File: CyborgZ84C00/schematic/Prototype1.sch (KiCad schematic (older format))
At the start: 13 parts, among them J1 Conn_Micro_SD, J2 Conn_I2C_Master, J3 Conn_AVR_UPDI, J4 Conn_USB_Serial, U1 Z84C00, U2 ATmega4809-P, U3 HM628128

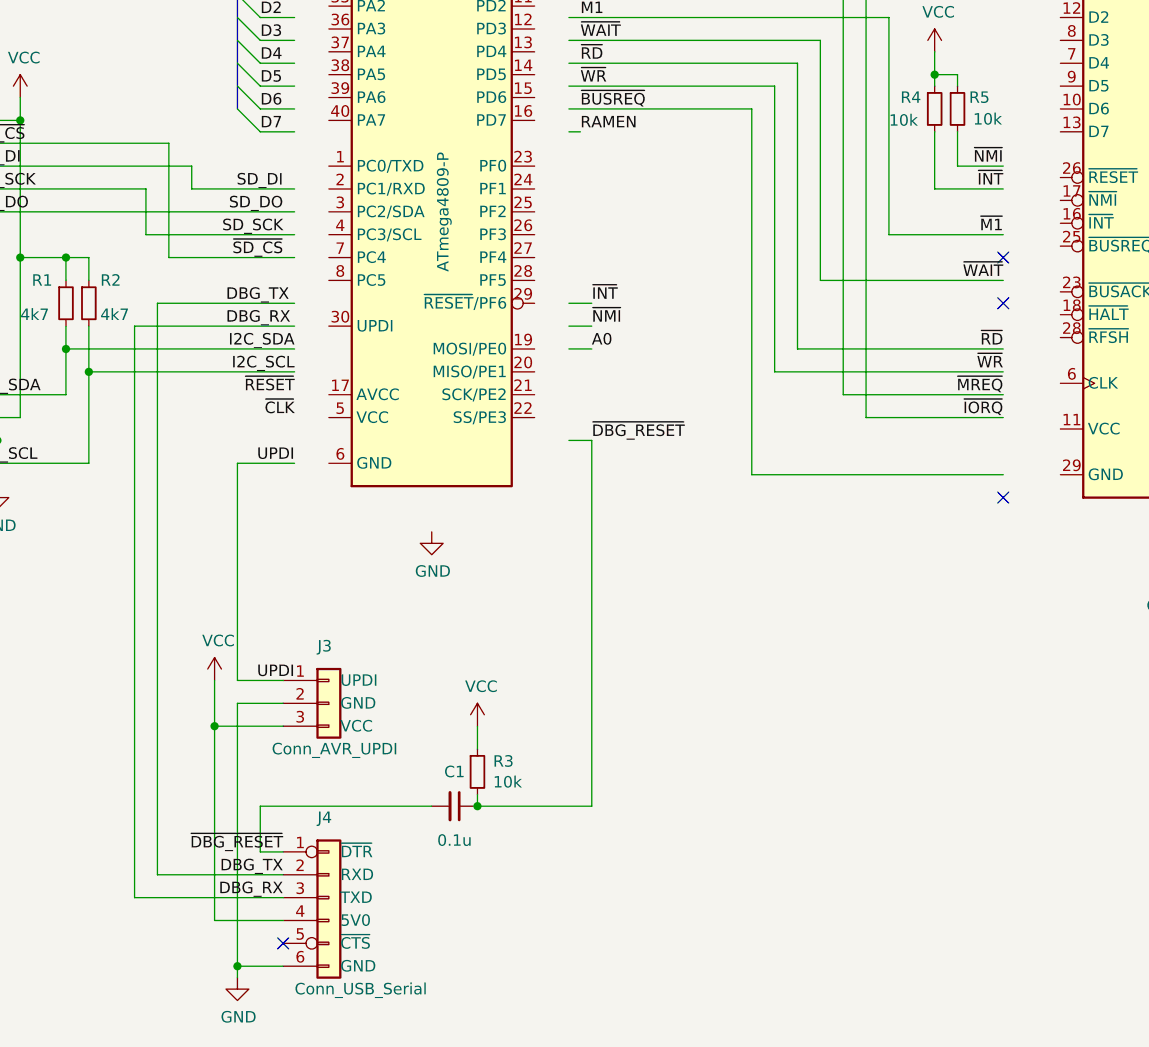
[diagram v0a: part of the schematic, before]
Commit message: [CyborgZ84C00] update debugger code
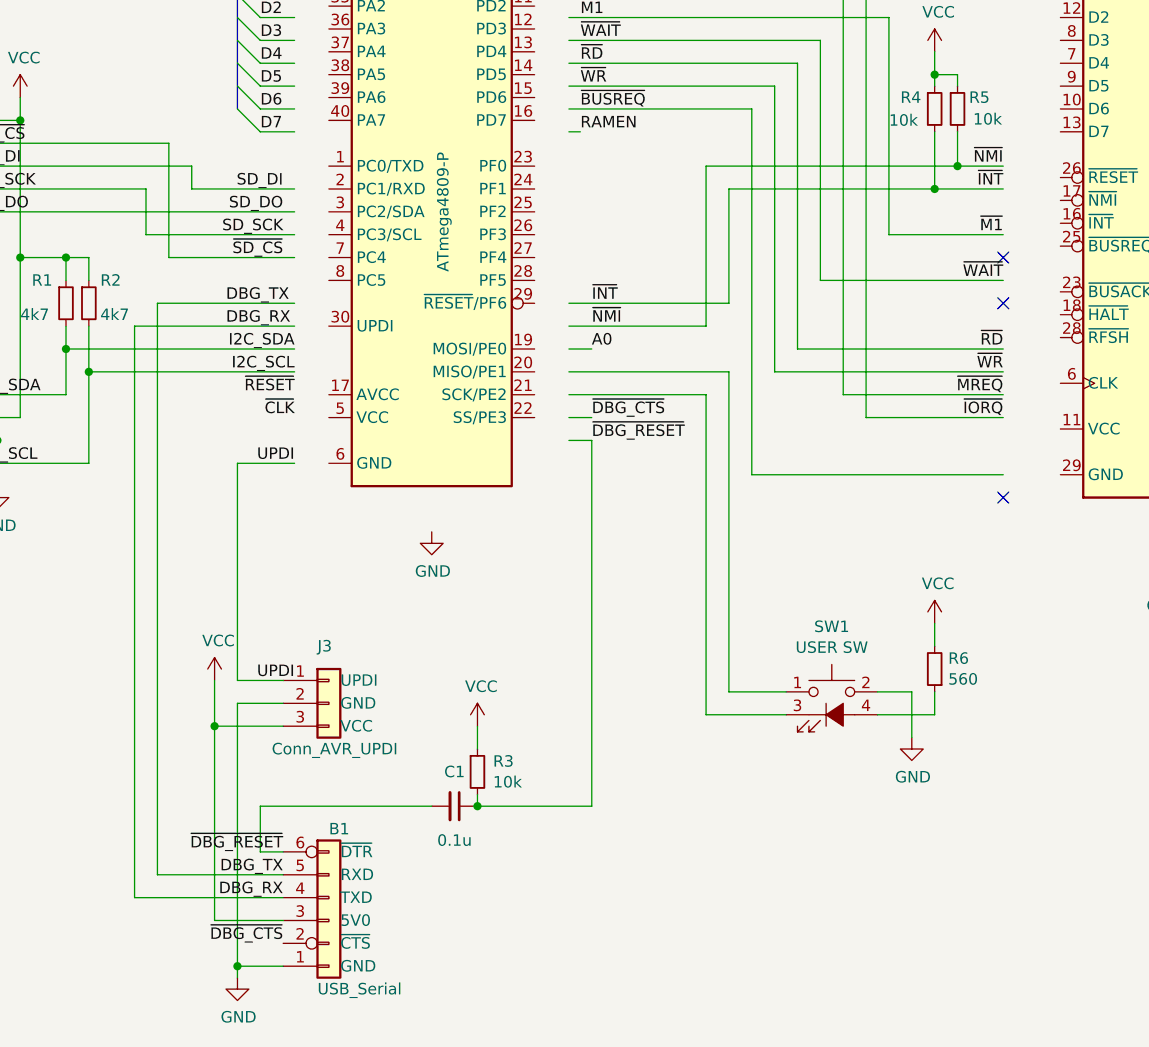
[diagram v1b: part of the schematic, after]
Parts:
- removed J4: Conn_USB_Serial, symbol 0-LocalLibrary:Conn_USB_Serial
- added B1: USB_Serial, 0-LocalLibrary:GY232V2, symbol 0-LocalLibrary:USB_Serial
- added R6: 560, symbol Device:R_Small
- added SW1: USER SW, 0-LocalLibrary:SW_PUSH-LED-12mm, symbol 0-LocalLibrary:SW_Push_LED
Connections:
- net labels added: ~DBG_CTS~
- wire segments 152 -> 168
- no-connect marks 5 -> 4
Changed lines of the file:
@@
 EESchema Schematic File Version 4
-LIBS:Prototype1-cache
 EELAYER 30 0
 EELAYER END
@@
 	3750 1550 3650 1550
 $Comp
-L 0-LocalLibrary:Conn_USB_Serial J4
-U 1 1 5DD41B19
-P 3200 5950
-F 0 "J4" H 3150 6300 50  0000 L CNN
-F 1 "Conn_USB_Serial" H 3050 5550 50  0000 L CNN
-F 2 "" H 3200 5950 50  0001 C CNN
-F 3 "~" H 3200 5950 50  0001 C CNN
-	1    3200 5950
-	1    0    0    -1
-$EndComp
-$Comp
 L Device:C_Small C1
 U 1 1 5DD45267
@@
 	1750 3950 1750 4150
 $Comp
-L power:GND #PWR?
+L power:GND #PWR013
 U 1 1 5DD8E08D
 P 9350 3350
-F 0 "#PWR?" H 9350 3100 50  0001 C CNN
+F 0 "#PWR013" H 9350 3100 50  0001 C CNN
 F 1 "GND" H 9355 3177 50  0000 C CNN
 F 2 "" H 9350 3350 50  0001 C CNN
@@
 Text Label 3000 5950 2    50   ~ 0
 DBG_RX
-NoConn ~ 3000 6150
-Wire Wire Line
-	4250 3350 4350 3350
-Text Label 4350 3350 0    50   ~ 0
-~INT~
-Wire Wire Line
-	4250 3450 4350 3450
 Text Label 4300 2600 0    50   ~ 0
 RAMEN
@@
 Wire Wire Line
 	5450 3750 6150 3750
-Text Label 4350 3450 0    50   ~ 0
-~NMI~
 Text Label 6150 2750 2    50   ~ 0
 ~NMI~
@@
 Wire Wire Line
 	5850 2850 6150 2850
+Wire Wire Line
+	4250 3350 4950 3350
+Wire Wire Line
+	4950 3350 4950 2850
+Wire Wire Line
+	4950 2850 5850 2850
+Connection ~ 5850 2850
+Wire Wire Line
+	4250 3450 4850 3450
+Wire Wire Line
+	4850 3450 4850 2750
+Wire Wire Line
+	4850 2750 5950 2750
+Connection ~ 5950 2750
+Text Label 4350 3450 0    50   ~ 0
+~NMI~
+Text Label 4350 3350 0    50   ~ 0
+~INT~
+Text Label 3000 6150 2    50   ~ 0
+~DBG_CTS~
+Text Label 4350 3850 0    50   ~ 0
+~DBG_CTS~
+Wire Wire Line
+	4250 3650 4950 3650
+Wire Wire Line
+	4250 3850 4350 3850
+Wire Wire Line
+	4250 3750 4850 3750
+$Comp
+L 0-LocalLibrary:SW_Push_LED SW1
+U 1 1 5FF4210E
+P 5400 5150
+F 0 "SW1" H 5400 5535 50  0000 C CNN
+F 1 "USER SW" H 5400 5444 50  0000 C CNN
+F 2 "0-LocalLibrary:SW_PUSH-LED-12mm" H 5400 5450 50  0001 C CNN
+F 3 "~" H 5400 5450 50  0001 C CNN
+	1    5400 5150
+	1    0    0    -1
+$EndComp
+$Comp
+L 0-LocalLibrary:USB_Serial B1
+U 1 1 5FF433B7
+P 3200 5950
+F 0 "B1" H 3200 6250 50  0000 L CNN
+F 1 "USB_Serial" H 3150 5550 50  0000 L CNN
+F 2 "0-LocalLibrary:GY232V2" H 3200 5950 50  0001 C CNN
+F 3 "~" H 3200 5950 50  0001 C CNN
+	1    3200 5950
+	1    0    0    -1
+$EndComp
+Wire Wire Line
+	4950 5050 5200 5050
+Wire Wire Line
+	4950 3650 4950 5050
+Wire Wire Line
+	4850 5150 5200 5150
+Wire Wire Line
+	4850 3750 4850 5150
+Wire Wire Line
+	5600 5050 5750 5050
+Wire Wire Line
+	5750 5050 5750 5250
+Wire Wire Line
+	5600 5150 5850 5150
+$Comp
+L Device:R_Small R6
+U 1 1 5FF76123
+P 5850 4950
+F 0 "R6" H 5791 4904 50  0000 R CNN
+F 1 "560" H 5791 4995 50  0000 R CNN
+F 2 "" H 5850 4950 50  0001 C CNN
+F 3 "~" H 5850 4950 50  0001 C CNN
+	1    5850 4950
+	-1   0    0    1
+$EndComp
+Wire Wire Line
+	5850 5050 5850 5150
+$Comp
+L power:VCC #PWR015
+U 1 1 5FF911BA
+P 5850 4750
+F 0 "#PWR015" H 5850 4600 50  0001 C CNN
+F 1 "VCC" H 5865 4923 50  0000 C CNN
+F 2 "" H 5850 4750 50  0001 C CNN
+F 3 "" H 5850 4750 50  0001 C CNN
+	1    5850 4750
+	1    0    0    -1
+$EndComp
+Wire Wire Line
+	5850 4750 5850 4850
 Wire Bus Line
 	7750 950  7750 2400
@@
 Wire Bus Line
 	7750 2800 7750 4750
+$Comp
+L power:GND #PWR014
+U 1 1 5FF9D78C
+P 5750 5250
+F 0 "#PWR014" H 5750 5000 50  0001 C CNN
+F 1 "GND" H 5755 5077 50  0000 C CNN
+F 2 "" H 5750 5250 50  0001 C CNN
+F 3 "" H 5750 5250 50  0001 C CNN
+	1    5750 5250
+	1    0    0    -1
+$EndComp
 $EndSCHEMATC

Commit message: [CyborgZ84C00] Update schematics symbols
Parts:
- removed B1: USB_Serial, 0-LocalLibrary:GY232V2, symbol 0-LocalLibrary:USB_Serial
- removed J1: Conn_Micro_SD, symbol 0-LocalLibrary:Conn_Micro_SD
- removed J2: Conn_I2C_Master, symbol 0-LocalLibrary:Conn_I2C_Master
- removed J3: Conn_AVR_UPDI, symbol 0-LocalLibrary:Conn_AVR_UPDI
- removed R1, R2: 4k7, symbol Device:R_Small
- removed U1: Z84C00, Package_DIP:DIP-40_W15.24mm, symbol 0-LocalLibrary:Z84C00
- removed U2: ATmega4809-P, Package_DIP:DIP-40_W15.24mm, symbol 0-LocalLibrary:ATmega4809-P
- removed U3: HM628128, Package_DIP:DIP-32_W15.24mm, symbol 0-LocalLibrary:HM628128
- added B2: USB_Serial, 0-LocalLibrary:GY232V2, symbol 0-LocalLibrary:USB_Serial
- added C2, C3, C7: 0.1u, Capacitor_THT:C_Disc_D3.4mm_W2.1mm_P2.50mm, symbol Device:C_Small
- added J1: Conn_AVR_UPDI, Connector_PinSocket_2.54mm:PinSocket_1x03_P2.54mm_Vertical, symbol 0-LocalLibrary:Conn_AVR_UPDI
- added J3: Conn_I2C_Master, Connector_PinSocket_2.54mm:PinSocket_1x04_P2.54mm_Vertical, symbol 0-LocalLibrary:Conn_I2C_Master
- added U1: ATmega4809-P, Package_DIP:DIP-40_W15.24mm, symbol 0-LocalLibrary:ATmega4809-P
- added U2: HM628128DLP-5, Package_DIP:DIP-32_W15.24mm_Socket, symbol 0-LocalLibrary:628128
- added U3: Z84C00, Package_DIP:DIP-40_W15.24mm, symbol 0-LocalLibrary:Z84C00
- C1: footprint (none) -> Capacitor_THT:C_Disc_D3.4mm_W2.1mm_P2.50mm
- R3, R6: footprint (none) -> Resistor_THT:R_Axial_DIN0204_L3.6mm_D1.6mm_P5.08mm_Horizontal
- R4, R5: value 10k -> 4k7; footprint (none) -> Resistor_THT:R_Axial_DIN0204_L3.6mm_D1.6mm_P5.08mm_Horizontal
- SW1: value USER SW -> TSD1265
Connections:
- net labels added: CLK, SCL, SDA, ~DBG_RTS~, ~RAM_E~, ~USR_LED~, ~USR_SW~
- net labels removed: I2C_SCL, I2C_SDA, RAMEN, UPDI, ~CLK~, ~DBG_CTS~
- wire segments 168 -> 155

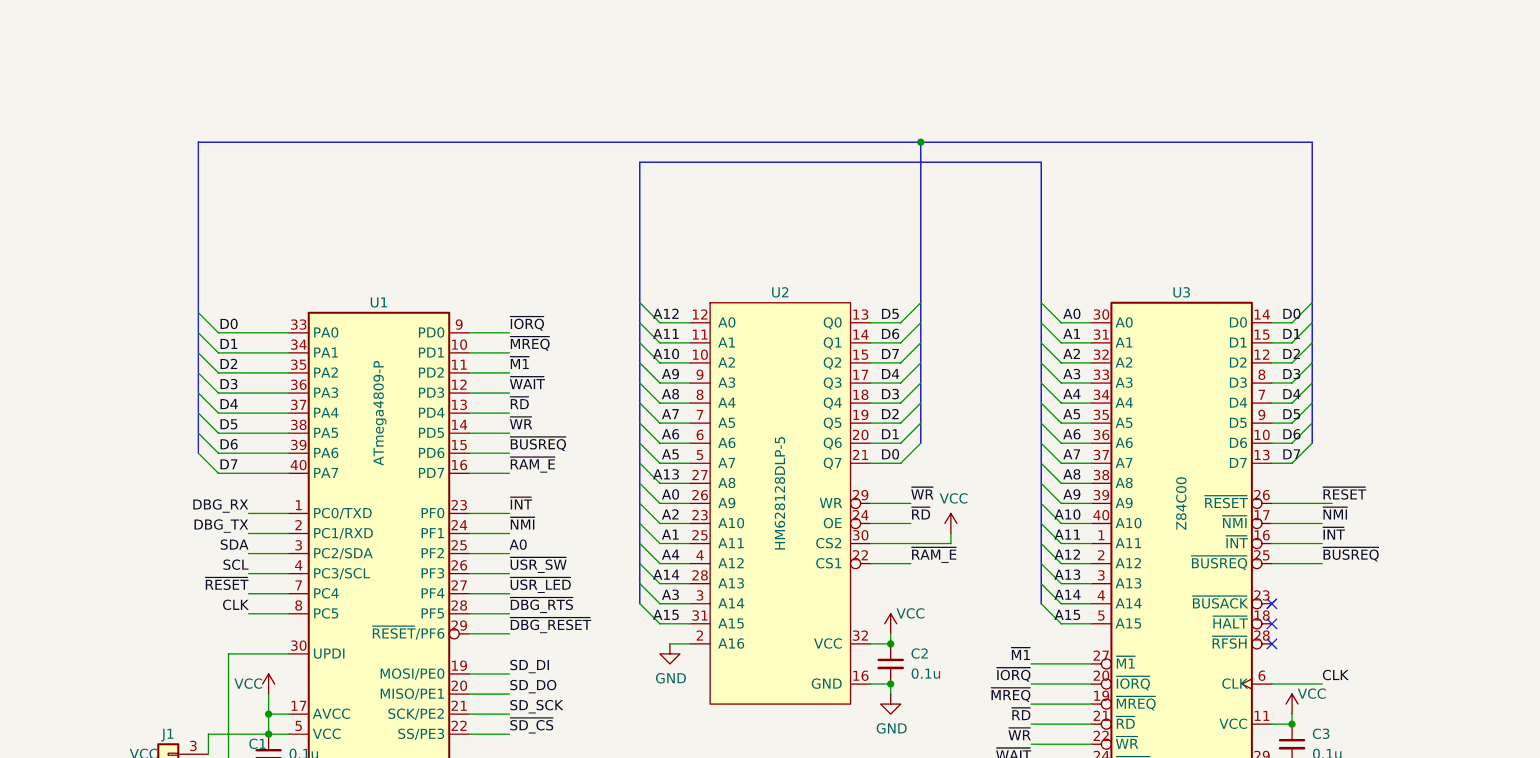
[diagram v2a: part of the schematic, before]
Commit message: [CyborgZ84C00] Update pin mapping
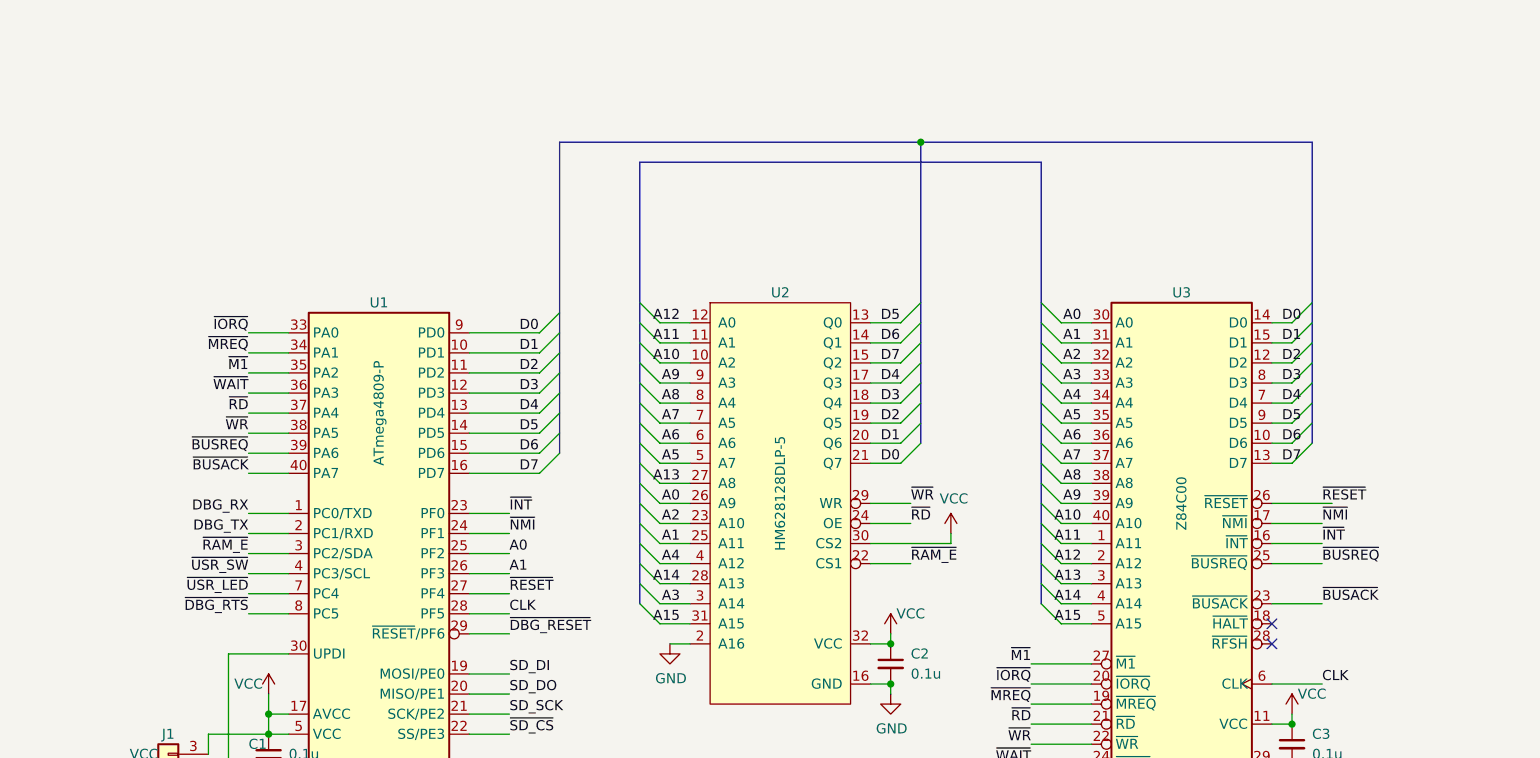
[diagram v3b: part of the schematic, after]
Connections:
- net labels added: ~BUSACK~
- wire segments 155 -> 156
- no-connect marks 4 -> 3
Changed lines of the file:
@@
 Text Label 3150 4100 0    50   ~ 0
 ~SD_CS~
-Text Label 1850 3300 2    50   ~ 0
-SCL
-Text Label 1850 3200 2    50   ~ 0
-SDA
 $Comp
 L power:GND #PWR019
@@
 $EndComp
 Entry Wire Line
-	1600 2000 1700 2100
-Entry Wire Line
-	1600 2100 1700 2200
-Entry Wire Line
-	1600 2200 1700 2300
-Entry Wire Line
-	1600 2300 1700 2400
-Entry Wire Line
-	1600 2400 1700 2500
-Entry Wire Line
-	1600 2500 1700 2600
-Entry Wire Line
-	1600 2600 1700 2700
-Entry Wire Line
-	1600 2700 1700 2800
+	3400 2000 3300 2100
+Entry Wire Line
+	3400 2100 3300 2200
+Entry Wire Line
+	3400 2200 3300 2300
+Entry Wire Line
+	3400 2300 3300 2400
+Entry Wire Line
+	3400 2400 3300 2500
+Entry Wire Line
+	3400 2500 3300 2600
+Entry Wire Line
+	3400 2600 3300 2700
+Entry Wire Line
+	3400 2700 3300 2800
 Text Label 3450 6150 2    50   ~ 0
 ~DBG_RTS~
@@
 Text Label 3150 3600 0    50   ~ 0
 ~DBG_RESET~
-Text Label 1850 3400 2    50   ~ 0
-~RESET~
-Text Label 1850 3500 2    50   ~ 0
+Text Label 3150 3500 0    50   ~ 0
 CLK
 $Comp
@@
 	2950 3300 3150 3300
 Wire Wire Line
-	2950 3400 3150 3400
-Wire Wire Line
-	2950 3500 3150 3500
+	2050 3400 1850 3400
+Wire Wire Line
+	2050 3500 1850 3500
 Wire Wire Line
 	2950 3600 3150 3600
@@
 	7050 4300 7050 4250
 Connection ~ 7050 4250
-Text Label 3150 3300 0    50   ~ 0
+Text Label 1850 3300 2    50   ~ 0
 ~USR_SW~
 Text Label 3150 3000 0    50   ~ 0
@@
 Wire Wire Line
 	3900 2850 4050 2850
-Text Label 1800 2800 2    50   ~ 0
+Text Label 3200 2800 0    50   ~ 0
 D7
-Text Label 1800 2700 2    50   ~ 0
+Text Label 3200 2700 0    50   ~ 0
 D6
-Text Label 1800 2600 2    50   ~ 0
+Text Label 3200 2600 0    50   ~ 0
 D5
-Text Label 1800 2500 2    50   ~ 0
+Text Label 3200 2500 0    50   ~ 0
 D4
-Text Label 1800 2400 2    50   ~ 0
+Text Label 3200 2400 0    50   ~ 0
 D3
-Text Label 1800 2300 2    50   ~ 0
+Text Label 3200 2300 0    50   ~ 0
 D2
-Text Label 1800 2200 2    50   ~ 0
+Text Label 3200 2200 0    50   ~ 0
 D1
-Text Label 1800 2100 2    50   ~ 0
+Text Label 3200 2100 0    50   ~ 0
 D0
 Wire Bus Line
@@
 	5900 2050 6050 2050
 Wire Wire Line
-	1700 2800 2050 2800
-Wire Wire Line
-	1700 2700 2050 2700
-Wire Wire Line
-	1700 2600 2050 2600
-Wire Wire Line
-	1700 2500 2050 2500
-Wire Wire Line
-	1700 2400 2050 2400
-Wire Wire Line
-	1700 2300 2050 2300
-Wire Wire Line
-	1700 2200 2050 2200
-Wire Wire Line
-	1700 2100 2050 2100
-Wire Bus Line
-	1600 1150 5200 1150
-Wire Wire Line
-	1850 3400 2050 3400
-Wire Wire Line
-	1850 3500 2050 3500
+	3300 2800 2950 2800
+Wire Wire Line
+	3300 2700 2950 2700
+Wire Wire Line
+	3300 2600 2950 2600
+Wire Wire Line
+	3300 2500 2950 2500
+Wire Wire Line
+	3300 2400 2950 2400
+Wire Wire Line
+	3300 2300 2950 2300
+Wire Wire Line
+	3300 2200 2950 2200
+Wire Wire Line
+	3300 2100 2950 2100
+Wire Wire Line
+	3150 3400 2950 3400
+Wire Wire Line
+	3150 3500 2950 3500
 Text Label 7200 3850 0    50   ~ 0
 CLK
 Wire Wire Line
-	2950 2100 3150 2100
-Text Label 3150 2100 0    50   ~ 0
+	2050 2100 1850 2100
+Text Label 1850 2100 2    50   ~ 0
 ~IORQ~
 Wire Wire Line
-	2950 2200 3150 2200
-Text Label 3150 2200 0    50   ~ 0
+	2050 2200 1850 2200
+Text Label 1850 2200 2    50   ~ 0
 ~MREQ~
 Wire Wire Line
-	2950 2300 3150 2300
-Text Label 3150 2300 0    50   ~ 0
+	2050 2300 1850 2300
+Text Label 1850 2300 2    50   ~ 0
 ~M1~
 Wire Wire Line
-	2950 2400 3150 2400
-Text Label 3150 2400 0    50   ~ 0
+	2050 2400 1850 2400
+Text Label 1850 2400 2    50   ~ 0
 ~WAIT~
 Wire Wire Line
-	2950 2500 3150 2500
-Text Label 3150 2500 0    50   ~ 0
+	2050 2500 1850 2500
+Text Label 1850 2500 2    50   ~ 0
 ~RD~
 Wire Wire Line
-	2950 2600 3150 2600
-Text Label 3150 2600 0    50   ~ 0
+	2050 2600 1850 2600
+Text Label 1850 2600 2    50   ~ 0
 ~WR~
 Wire Wire Line
-	2950 2700 3150 2700
-Text Label 3150 2700 0    50   ~ 0
+	2050 2700 1850 2700
+Text Label 1850 2700 2    50   ~ 0
 ~BUSREQ~
 Wire Wire Line
-	2950 2800 3150 2800
-Text Label 3150 2800 0    50   ~ 0
+	2050 2800 1850 2800
+Text Label 1850 3200 2    50   ~ 0
 ~RAM_E~
 Wire Wire Line
@@
 Text Label 3150 3200 0    50   ~ 0
 A0
-Text Label 3150 3400 0    50   ~ 0
+Text Label 1850 3400 2    50   ~ 0
 ~USR_LED~
-Text Label 3150 3500 0    50   ~ 0
+Text Label 1850 3500 2    50   ~ 0
 ~DBG_RTS~
 $Comp
@@
 	-1   0    0    -1
 $EndComp
-NoConn ~ 6950 3450
 NoConn ~ 6950 3550
 NoConn ~ 6950 3650
@@
 $EndComp
 Wire Bus Line
+	3400 1150 5200 1150
+Text Label 3150 3400 0    50   ~ 0
+~RESET~
+Text Label 1850 2800 2    50   ~ 0
+~BUSACK~
+Wire Wire Line
+	6950 3450 7200 3450
+Wire Bus Line
 	5200 1150 5200 2650
 Wire Bus Line
-	1600 1150 1600 2700
+	3400 1150 3400 2700
 Wire Bus Line
 	7150 1150 7150 2650
@@
 Wire Bus Line
 	5800 1250 5800 3450
+Text Label 7200 3450 0    50   ~ 0
+~BUSACK~
+Text Label 3150 3300 0    50   ~ 0
+A1
 $EndSCHEMATC
